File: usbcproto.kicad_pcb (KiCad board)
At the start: 2 copper layers, 30 x 30 mm, 26 parts, among them U1 STM32F103RETx, U2 MIC5219-3.3YM5, X1 VAL**, Y1 Crystal_GND2_Small

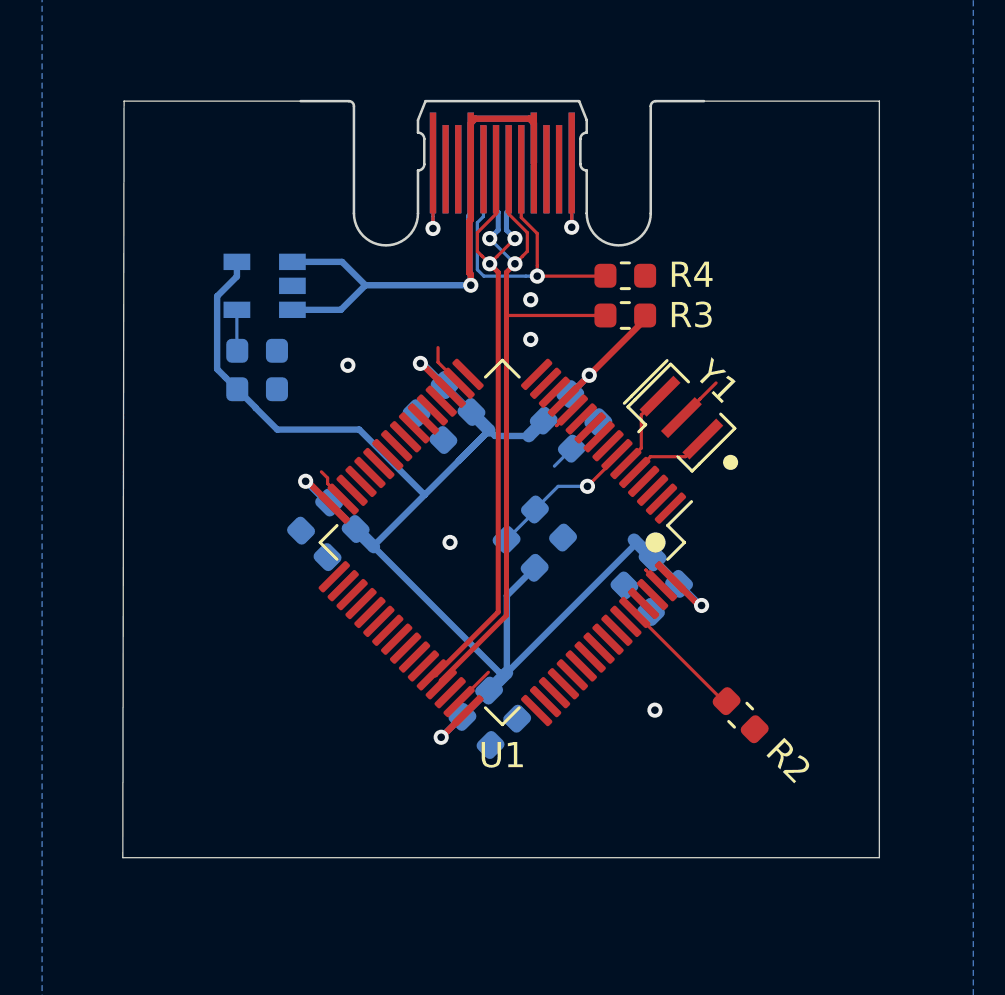
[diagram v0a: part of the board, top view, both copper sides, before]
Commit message: Route pins and RGB LED.
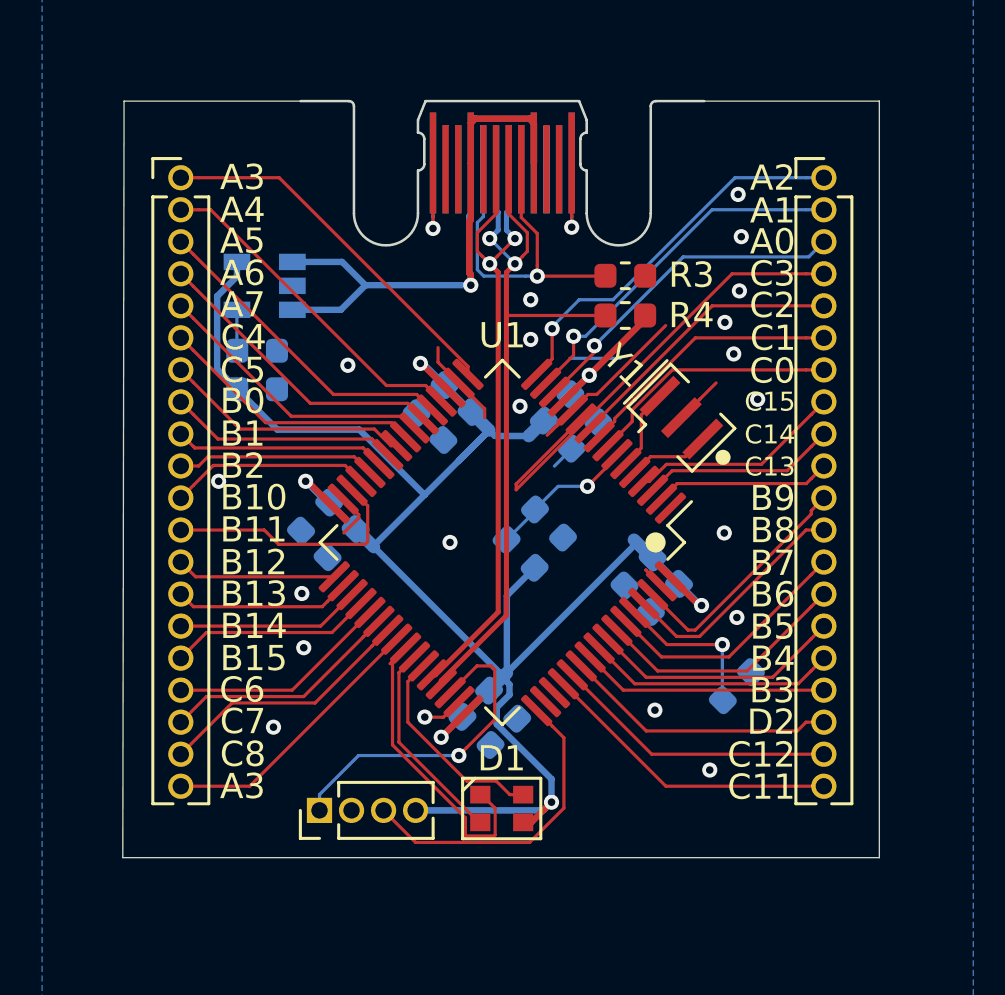
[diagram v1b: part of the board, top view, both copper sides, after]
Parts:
- added D1: FM-B2020RGBA-HG, fm-b2020rgba-hg:FM-B2020RGBA-HG, F.Cu at (127.8, 102.8)
- added J1: Conn_01x04_Male, Connector_PinHeader_1.27mm:PinHeader_1x04_P1.27mm_Vertical, F.Cu at (120.5, 102.9)
- added J2: Conn_01x20_Male, Connector_PinHeader_1.27mm:PinHeader_1x20_P1.27mm_Vertical, F.Cu at (115.0, 77.8)
- added J3: Conn_01x20_Male, Connector_PinHeader_1.27mm:PinHeader_1x20_P1.27mm_Vertical, F.Cu at (140.6, 77.8)
- R2: moved to B.Cu
- X1: value VAL** -> PCB-USB-C
- moved R2 1.16 mm to (137.1, 98.0), turned to 45 degrees
- renumbered R4 to R3, R3 to R4
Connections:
- net Net-(U1-Pad50) renamed /PA15
- net Net-(U1-Pad51) renamed /PC10
- U1 pad 10: Net-(U1-Pad10) -> /PC2
- U1 pad 11: Net-(U1-Pad11) -> /PC3
- U1 pad 14: Net-(U1-Pad14) -> /PA0
- U1 pad 15: Net-(U1-Pad15) -> /PA1
- U1 pad 16: Net-(U1-Pad16) -> /PA2
- U1 pad 17: Net-(U1-Pad17) -> /PA3
- U1 pad 2: Net-(U1-Pad2) -> /PC13
- U1 pad 20: Net-(U1-Pad20) -> /PA4
- U1 pad 21: Net-(U1-Pad21) -> /PA5
- U1 pad 22: Net-(U1-Pad22) -> /PA6
- U1 pad 23: Net-(U1-Pad23) -> /PA7
- U1 pad 24: Net-(U1-Pad24) -> /PC4
- U1 pad 25: Net-(U1-Pad25) -> /PC5
- U1 pad 26: Net-(U1-Pad26) -> /PB0
- U1 pad 27: Net-(U1-Pad27) -> /PB1
- U1 pad 28: Net-(U1-Pad28) -> /PB2
- U1 pad 29: Net-(U1-Pad29) -> /PB10
- U1 pad 3: Net-(U1-Pad3) -> /PC14
- U1 pad 30: Net-(U1-Pad30) -> /PB11
- U1 pad 33: Net-(U1-Pad33) -> /PB12
- U1 pad 34: Net-(U1-Pad34) -> /PB13
- U1 pad 35: Net-(U1-Pad35) -> /PB14
- U1 pad 36: Net-(U1-Pad36) -> /PB15
- U1 pad 37: Net-(U1-Pad37) -> /PC6
- U1 pad 38: Net-(U1-Pad38) -> /PC7
- U1 pad 39: Net-(U1-Pad39) -> /PC8
- U1 pad 4: Net-(U1-Pad4) -> /PC15
- U1 pad 40: Net-(U1-Pad40) -> /PC9
- U1 pad 41: Net-(U1-Pad41) -> /PA8
- U1 pad 42: Net-(U1-Pad42) -> /PA9
- U1 pad 43: Net-(U1-Pad43) -> /PA10
- U1 pad 46: Net-(U1-Pad46) -> SWDIO
- U1 pad 49: Net-(U1-Pad49) -> SWCLK
- U1 pad 52: Net-(U1-Pad52) -> /PC11
- U1 pad 53: Net-(U1-Pad53) -> /PC12
- U1 pad 54: Net-(U1-Pad54) -> /PD2
- U1 pad 55: Net-(U1-Pad55) -> /PB3
- U1 pad 56: Net-(U1-Pad56) -> /PB4
- U1 pad 57: Net-(U1-Pad57) -> /PB5
- U1 pad 58: Net-(U1-Pad58) -> /PB6
- U1 pad 59: Net-(U1-Pad59) -> /PB7
- U1 pad 61: Net-(U1-Pad61) -> /PB8
- U1 pad 62: Net-(U1-Pad62) -> /PB9
- U1 pad 8: Net-(U1-Pad8) -> /PC0
- U1 pad 9: Net-(U1-Pad9) -> /PC1
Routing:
- net /PC3: track 0.00 -> 19.6 mm
- net /PA2: track 0.00 -> 15.4 mm, vias 0 -> 1
- net /PA3: track 0.00 -> 14.8 mm
- net /PA1: track 0.00 -> 14.3 mm, vias 0 -> 1
- net /PA4: track 0.00 -> 13.5 mm
- net /PA0: track 0.00 -> 13.3 mm, vias 0 -> 1
- net +3V3: track 44.4 -> 57.6 mm, vias 0 -> 1
- net SWDIO: track 0.00 -> 13.1 mm, vias 0 -> 1
- net /PA8: track 0.00 -> 12.8 mm
- net /PA5: track 0.00 -> 12.7 mm
- net SWCLK: track 0.00 -> 12.6 mm
- net /PC11: track 0.00 -> 12.0 mm
- net /PA6: track 0.00 -> 12.0 mm
- net GND: track 20.1 -> 31.9 mm, vias 7 -> 22
- net /PC12: track 0.00 -> 11.3 mm
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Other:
- board text added: "A0"
- board text added: "A1"
- board text added: "A2"
- board text added: "A3"
- board text added: "A4"
- board text added: "A5"
- board text added: "A6"
- board text added: "A7"
- board text added: "B0"
- board text added: "B1"
- board text added: "B10"
- board text added: "B11"
- board text added: "B12"
- board text added: "B13"
- board text added: "B14"
- board text added: "B15"
- board text added: "B2"
- board text added: "B3"
- board text added: "B4"
- board text added: "B5"
- board text added: "B6"
- board text added: "B7"
- board text added: "B8"
- board text added: "B9"
- board text added: "C0"
- board text added: "C1"
- board text added: "C11"
- board text added: "C12"
- board text added: "C13"
- board text added: "C14"
- board text added: "C15"
- board text added: "C2"
- board text added: "C3"
- board text added: "C4"
- board text added: "C5"
- board text added: "C6"
- board text added: "C7"
- board text added: "C8"
- board text added: "D2"
